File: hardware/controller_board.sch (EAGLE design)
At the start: 121 parts, among them J1 FRSKY-GIMBAL-FRYSKY, J11 USB-MICROA-AMPHENOL-10118192-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, J2 FRSKY-GIMBAL-FRYSKY, J3 USB-MICROB-EDAC-690-005-299-0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, J4 AVR_SPI_PRG_6NS, J8 FRSKY-GIMBAL-2X-SERVO, J9 FRSKY-GIMBAL-2X-SERVO, P6 10K, U1 ATMEGA128RFA1, U2 DPDT-X2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

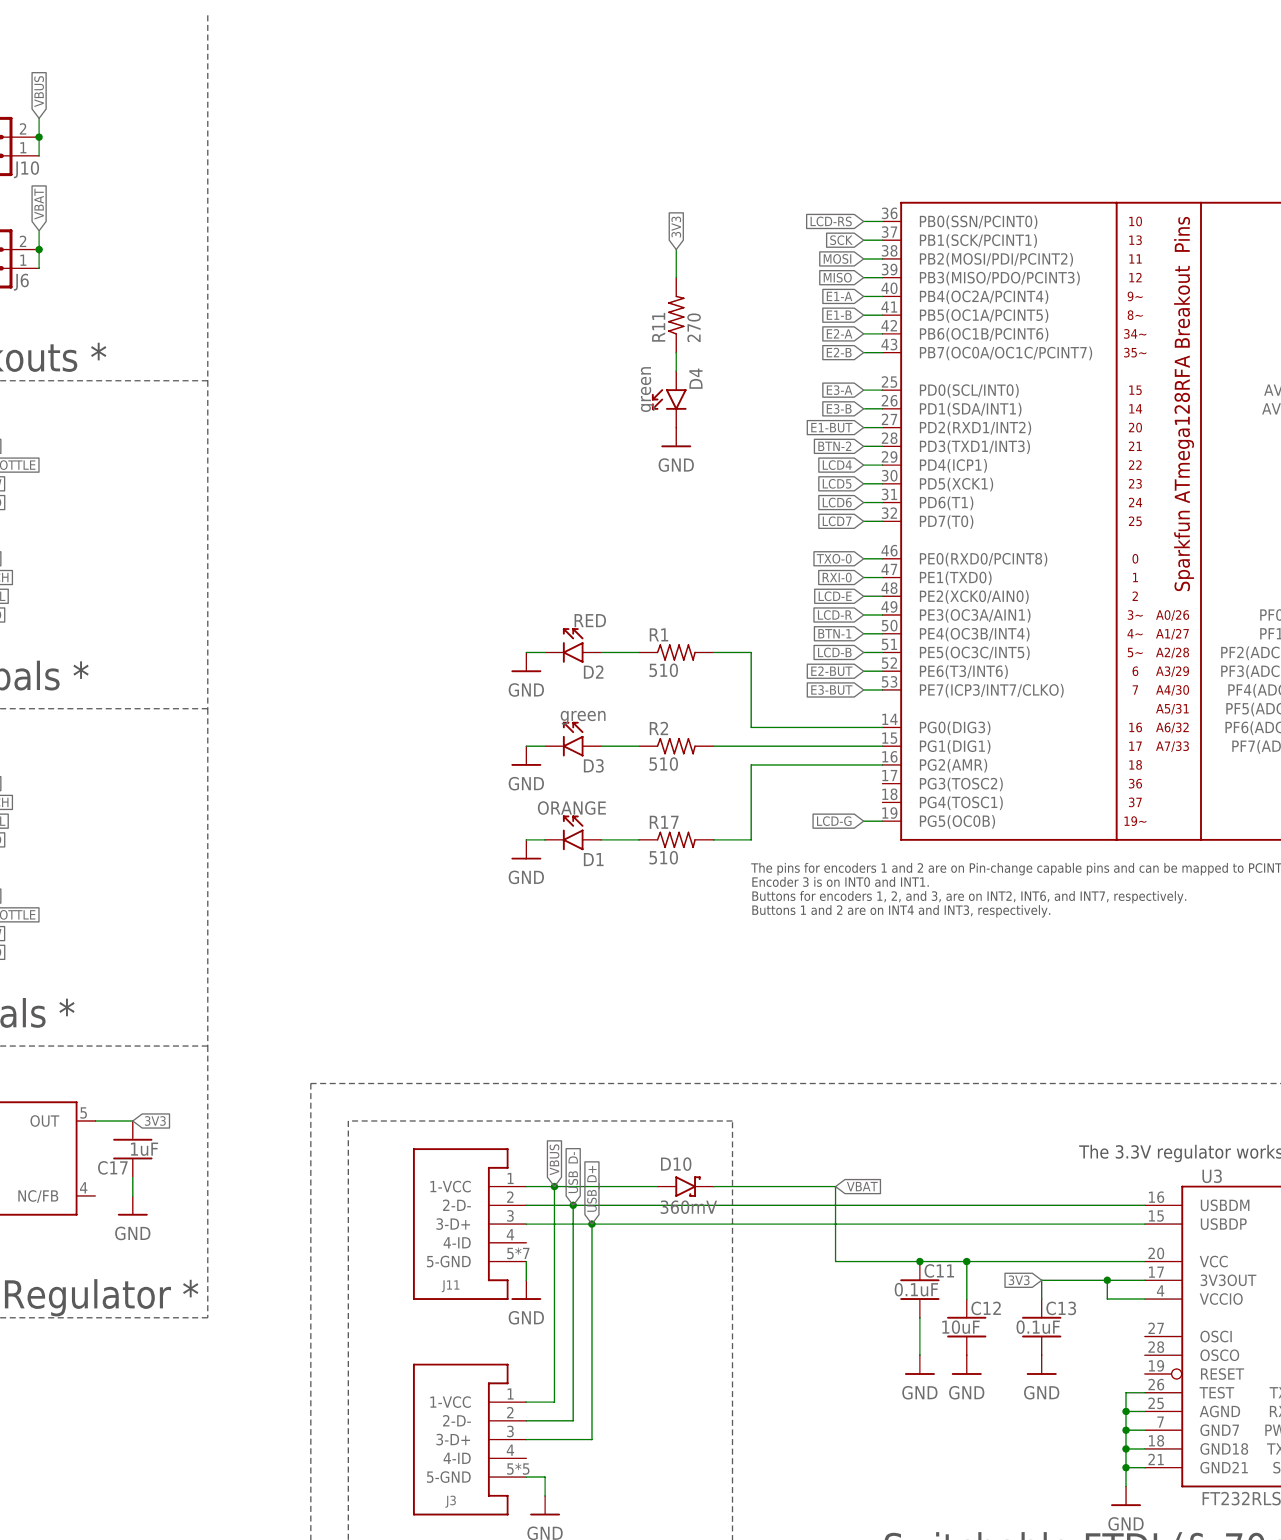
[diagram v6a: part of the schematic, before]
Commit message: fix outline
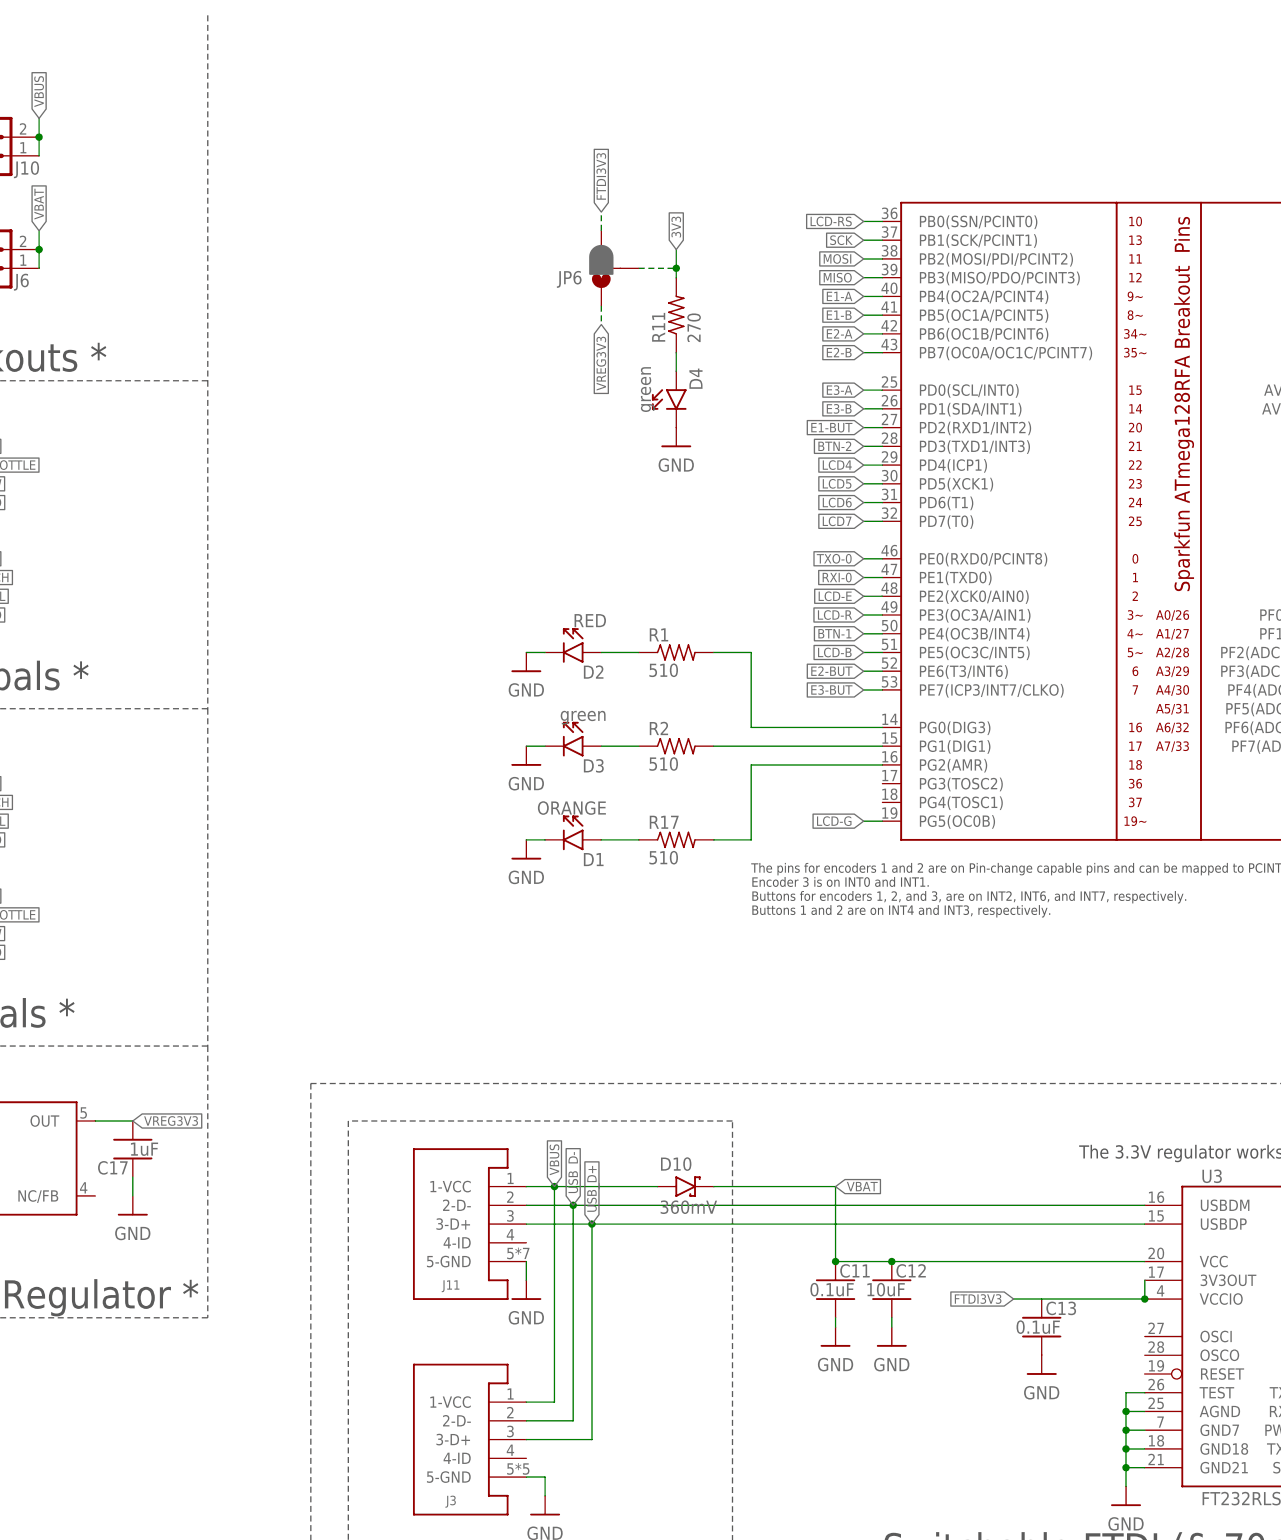
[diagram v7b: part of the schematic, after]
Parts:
- added JP6: JUMPER-SMT_3_1-NC_PASTE_NO-SILK, RemoteParts:JUMPER-SMT_3_1-NC_PASTE_NO-SILK
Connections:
- new net FTDI3V3: C13.1, JP6.3, U3.3V3OUT, U3.VCCIO
- new net VREG3V3: C17.2, JP6.1, U5.OUT
- net 3V3: now also JP6.2; no longer C13.1, C17.2, U3.3V3OUT, U3.VCCIO, U5.OUT
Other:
- moved on the sheet: C11, C12
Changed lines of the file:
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@@
 <part name="GND4" library="quadparts_prebuilt" deviceset="GND" device=""/>
 <part name="U5" library="quadparts_prebuilt" deviceset="TPS73633-DBVT" device="3V3" value="3.3V"/>
+<part name="JP6" library="RemoteParts" deviceset="JUMPER-SMT_3_1-NC_PASTE" device="_NO-SILK"/>
 </parts>
 <sheets>
@@
 <instance part="GND26" gate="1" x="187.96" y="73.66"/>
 <instance part="U3" gate="G$1" x="205.74" y="96.52"/>
-<instance part="GND28" gate="1" x="160.02" y="91.44"/>
-<instance part="GND30" gate="1" x="166.37" y="91.44"/>
+<instance part="GND28" gate="1" x="148.59" y="95.25"/>
+<instance part="GND30" gate="1" x="156.21" y="95.25"/>
 <instance part="R6" gate="G$1" x="240.03" y="101.6" rot="R90"/>
 <instance part="R7" gate="G$1" x="248.92" y="101.6" rot="R90"/>
-<instance part="C11" gate="G$1" x="160.02" y="104.14"/>
-<instance part="C12" gate="G$1" x="166.37" y="99.06"/>
+<instance part="C11" gate="G$1" x="148.59" y="104.14"/>
+<instance part="C12" gate="G$1" x="156.21" y="104.14"/>
 <instance part="C13" gate="G$1" x="176.53" y="99.06"/>
 <instance part="D5" gate="G$1" x="248.92" y="90.17" rot="R270"/>
@@
 <instance part="GND4" gate="1" x="22.86" y="118.11"/>
 <instance part="U5" gate="G$1" x="27.94" y="113.03"/>
+<instance part="JP6" gate="G$1" x="116.84" y="241.3" rot="R180"/>
 </instances>
 <busses>
@@
 <pinref part="GND28" gate="1" pin="GND"/>
 <pinref part="C11" gate="G$1" pin="2"/>
-<wire x1="160.02" y1="99.06" x2="160.02" y2="93.98" width="0.1524" layer="91"/>
+<wire x1="148.59" y1="99.06" x2="148.59" y2="97.79" width="0.1524" layer="91"/>
 </segment>
 <segment>
 <pinref part="GND30" gate="1" pin="GND"/>
 <pinref part="C12" gate="G$1" pin="2"/>
+<wire x1="156.21" y1="99.06" x2="156.21" y2="97.79" width="0.1524" layer="91"/>
 </segment>
 <segment>
@@
 </segment>
 <segment>
-<wire x1="190.5" y1="104.14" x2="185.42" y2="104.14" width="0.1524" layer="91"/>
-<wire x1="185.42" y1="104.14" x2="176.53" y2="104.14" width="0.1524" layer="91"/>
-<wire x1="176.53" y1="104.14" x2="176.53" y2="101.6" width="0.1524" layer="91"/>
-<pinref part="U3" gate="G$1" pin="3V3OUT"/>
-<pinref part="C13" gate="G$1" pin="1"/>
-<label x="176.53" y="104.14" size="1.27" layer="95" rot="R180" xref="yes"/>
-<wire x1="185.42" y1="101.6" x2="190.5" y2="101.6" width="0.1524" layer="91"/>
-<pinref part="U3" gate="G$1" pin="VCCIO"/>
-<wire x1="185.42" y1="104.14" x2="185.42" y2="101.6" width="0.1524" layer="91"/>
-<junction x="185.42" y="104.14"/>
-</segment>
-<segment>
 <pinref part="R11" gate="G$1" pin="2"/>
 <label x="127" y="243.84" size="1.27" layer="95" rot="R90" xref="yes"/>
-<wire x1="127" y1="240.03" x2="127" y2="243.84" width="0.1524" layer="91"/>
+<wire x1="127" y1="240.03" x2="127" y2="241.3" width="0.1524" layer="91"/>
+<pinref part="JP6" gate="G$1" pin="2"/>
+<wire x1="127" y1="241.3" x2="127" y2="243.84" width="0.1524" layer="91"/>
+<wire x1="121.92" y1="241.3" x2="127" y2="241.3" width="0.1524" layer="91" style="longdash"/>
+<junction x="127" y="241.3"/>
 </segment>
 <segment>
@@
 <wire x1="26.67" y1="171.45" x2="30.48" y2="171.45" width="0.1524" layer="91"/>
 <label x="30.48" y="171.45" size="1.27" layer="95" xref="yes"/>
-</segment>
-<segment>
-<pinref part="C17" gate="G$1" pin="2"/>
-<pinref part="U5" gate="G$1" pin="OUT"/>
-<wire x1="48.26" y1="125.73" x2="53.34" y2="125.73" width="0.1524" layer="91"/>
-<label x="53.34" y="125.73" size="1.27" layer="95" xref="yes"/>
 </segment>
 </net>
@@
 <net name="VBAT" class="1">
 <segment>
-<wire x1="160.02" y1="106.68" x2="166.37" y2="106.68" width="0.1524" layer="91"/>
-<wire x1="166.37" y1="106.68" x2="190.5" y2="106.68" width="0.1524" layer="91"/>
-<wire x1="166.37" y1="101.6" x2="166.37" y2="106.68" width="0.1524" layer="91"/>
-<junction x="166.37" y="106.68"/>
+<wire x1="148.59" y1="106.68" x2="156.21" y2="106.68" width="0.1524" layer="91"/>
+<wire x1="156.21" y1="106.68" x2="190.5" y2="106.68" width="0.1524" layer="91"/>
+<junction x="156.21" y="106.68"/>
 <pinref part="C12" gate="G$1" pin="1"/>
 <pinref part="C11" gate="G$1" pin="1"/>
@@
 <pinref part="D10" gate="G$1" pin="C"/>
 <wire x1="132.08" y1="116.84" x2="148.59" y2="116.84" width="0.1524" layer="91"/>
-<wire x1="148.59" y1="106.68" x2="160.02" y2="106.68" width="0.1524" layer="91"/>
-<junction x="160.02" y="106.68"/>
+<junction x="148.59" y="106.68"/>
 <label x="148.59" y="116.84" size="1.27" layer="95" xref="yes"/>
 </segment>
@@
 </segment>
 </net>
+<net name="FTDI3V3" class="1">
+<segment>
+<wire x1="190.5" y1="104.14" x2="190.5" y2="101.6" width="0.1524" layer="91"/>
+<wire x1="190.5" y1="101.6" x2="176.53" y2="101.6" width="0.1524" layer="91"/>
+<wire x1="172.72" y1="101.6" x2="176.53" y2="101.6" width="0.1524" layer="91"/>
+<pinref part="U3" gate="G$1" pin="3V3OUT"/>
+<pinref part="C13" gate="G$1" pin="1"/>
+<label x="172.72" y="101.6" size="1.27" layer="95" rot="R180" xref="yes"/>
+<pinref part="U3" gate="G$1" pin="VCCIO"/>
+<junction x="190.5" y="101.6"/>
+</segment>
+<segment>
+<pinref part="JP6" gate="G$1" pin="3"/>
+<wire x1="116.84" y1="246.38" x2="116.84" y2="248.92" width="0.1524" layer="91" style="longdash"/>
+<label x="116.84" y="248.92" size="1.27" layer="95" rot="R90" xref="yes"/>
+</segment>
+</net>
+<net name="VREG3V3" class="1">
+<segment>
+<pinref part="C17" gate="G$1" pin="2"/>
+<pinref part="U5" gate="G$1" pin="OUT"/>
+<wire x1="48.26" y1="125.73" x2="53.34" y2="125.73" width="0.1524" layer="91"/>
+<label x="53.34" y="125.73" size="1.27" layer="95" xref="yes"/>
+</segment>
+<segment>
+<pinref part="JP6" gate="G$1" pin="1"/>
+<wire x1="116.84" y1="236.22" x2="116.84" y2="233.68" width="0.1524" layer="91" style="longdash"/>
+<label x="116.84" y="233.68" size="1.27" layer="95" rot="R270" xref="yes"/>
+</segment>
+</net>
